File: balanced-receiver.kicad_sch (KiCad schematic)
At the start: 51 parts, among them J1 NC3FAH2, J2 Barrel_Jack_Switch, J3 Screw_Terminal_01x02, J4 Screw_Terminal_01x02, J5 Screw_Terminal_01x02, J6 Screw_Terminal_01x02, J7 Screw_Terminal_01x02, J8 Conn_01x02_Pin, Q1 Q_PMOS_GDS, U1 THAT1240, U2 TPS62932, U3 LM2776

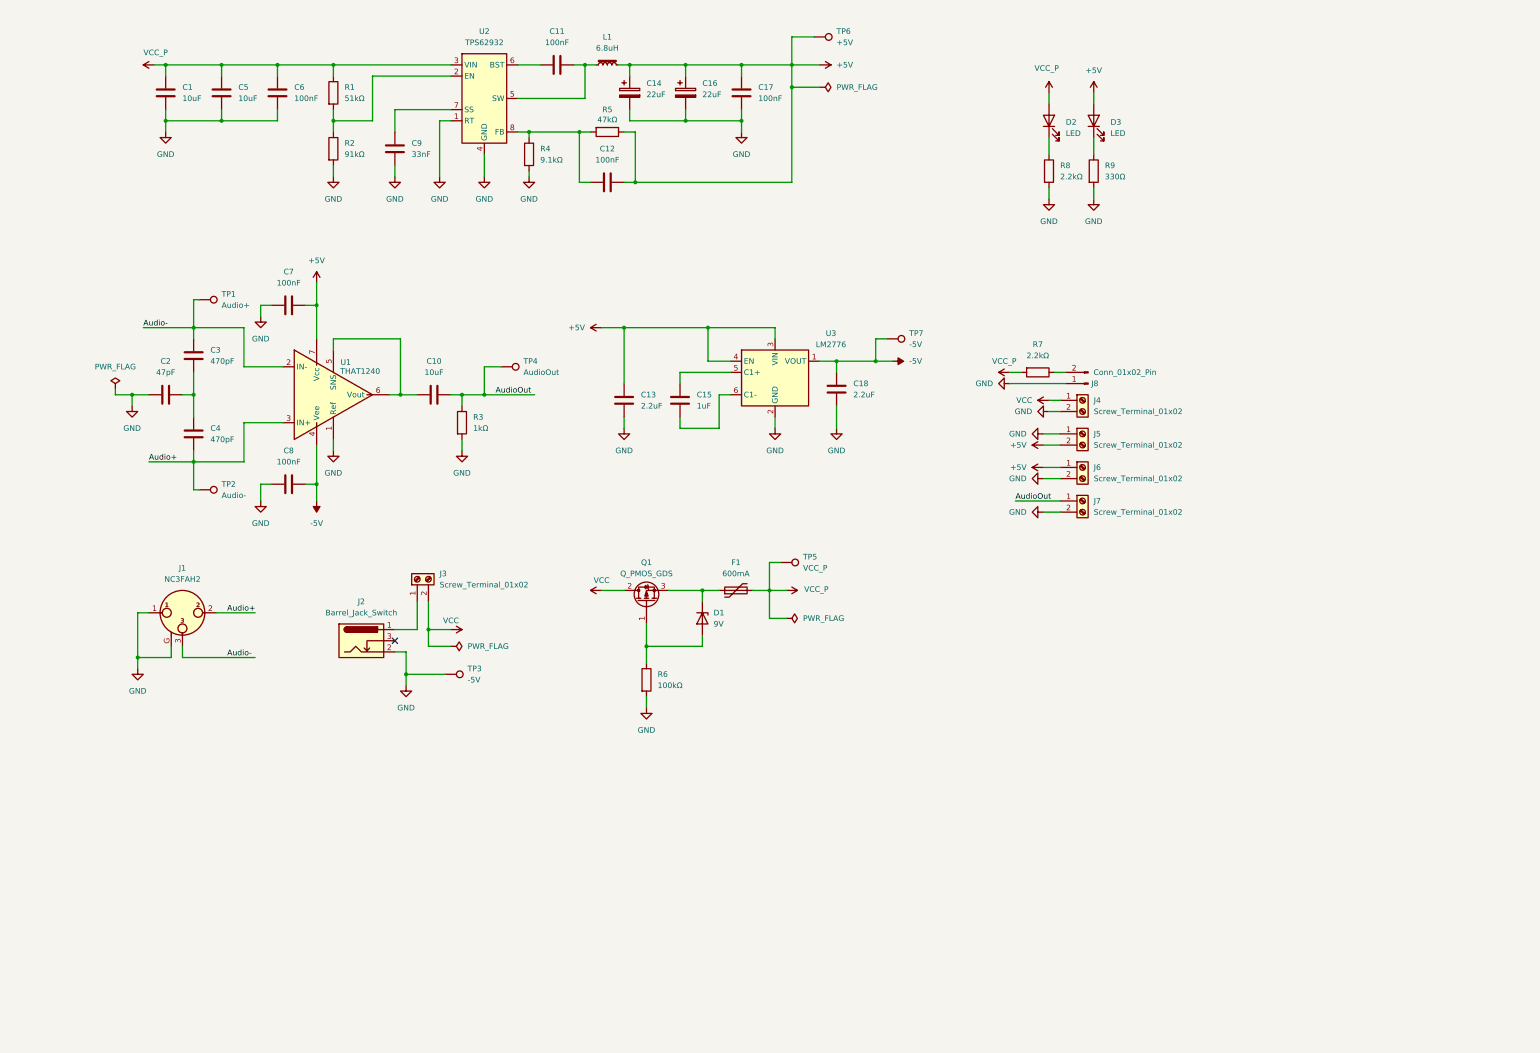
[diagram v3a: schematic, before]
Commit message: Added analog schemas
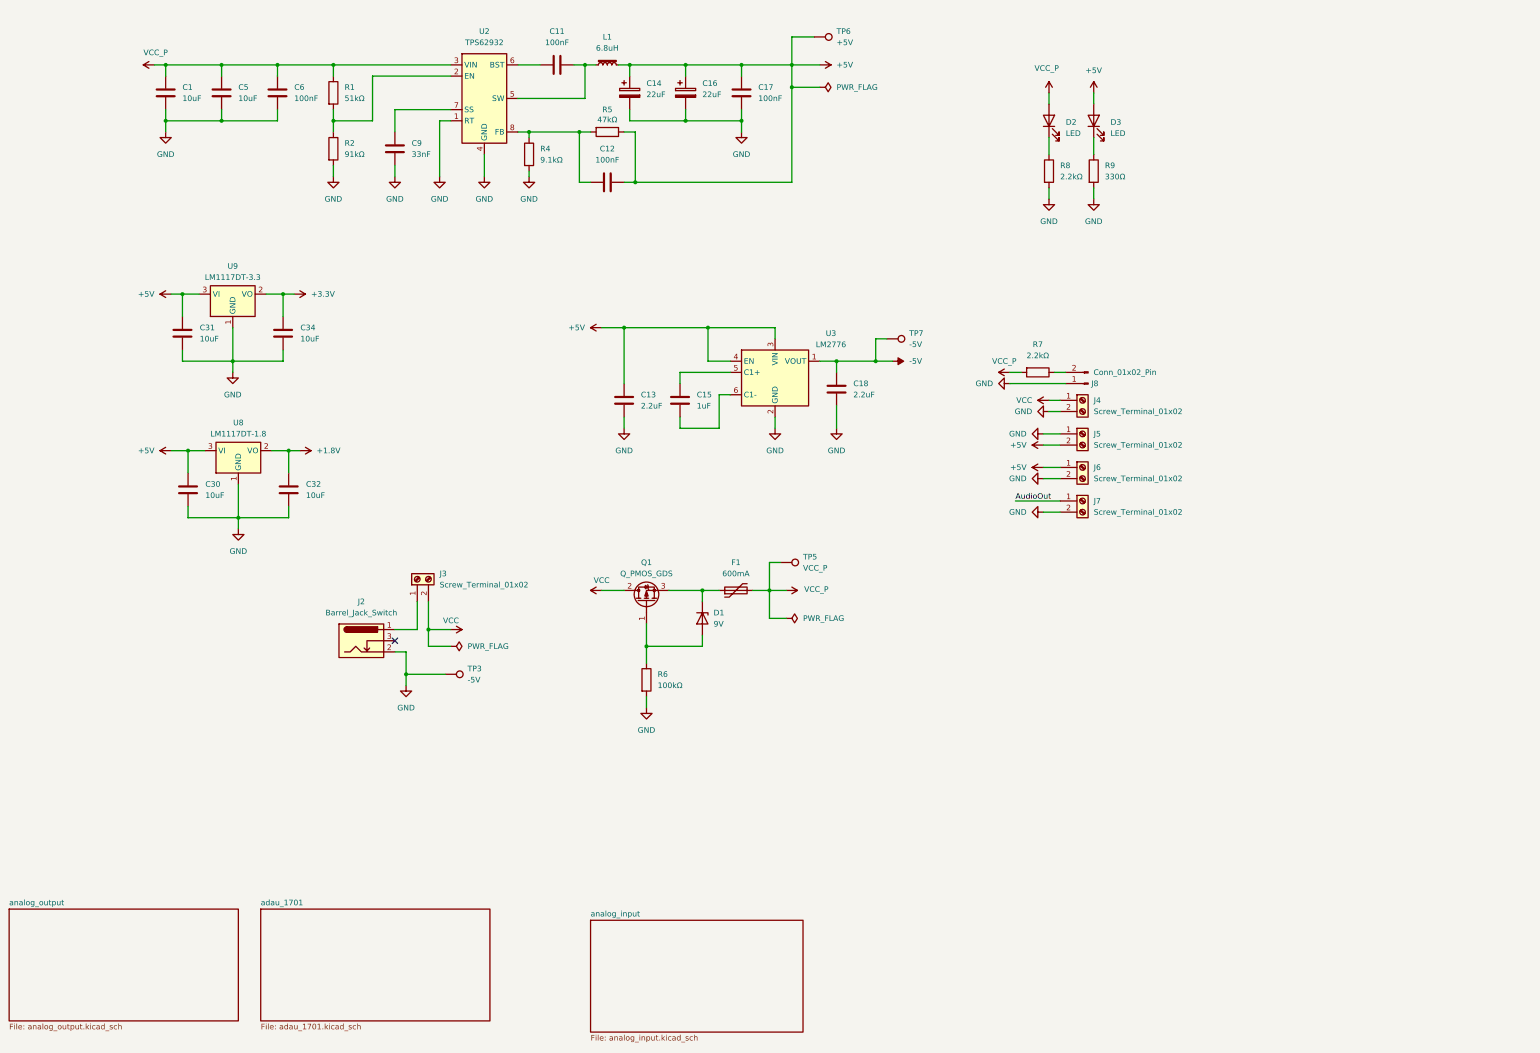
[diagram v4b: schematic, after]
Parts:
- removed C10: 10uF, Capacitor_SMD:C_0805_2012Metric_Pad1.18x1.45mm_HandSolder, symbol Device:C
- removed C2: 47pF, Capacitor_SMD:C_0805_2012Metric_Pad1.18x1.45mm_HandSolder, symbol Device:C
- removed C3, C4: 470pF, Capacitor_SMD:C_0805_2012Metric_Pad1.18x1.45mm_HandSolder, symbol Device:C
- removed C7, C8: 100nF, Capacitor_SMD:C_0805_2012Metric_Pad1.18x1.45mm_HandSolder, symbol Device:C
- removed J1: NC3FAH2, balanced-receiver:Jack_XLR_Neutrik_NC3FAH2_Horizontal, symbol Connector_Audio:NC3FAH2
- removed R3: 1kΩ, Resistor_SMD:R_0805_2012Metric_Pad1.20x1.40mm_HandSolder, symbol Device:R
- removed TP1: Audio+, TestPoint:TestPoint_Pad_D1.0mm, symbol Connector:TestPoint
- removed TP2: Audio-, TestPoint:TestPoint_Pad_D1.0mm, symbol Connector:TestPoint
- removed TP4: AudioOut, TestPoint:TestPoint_Pad_D1.0mm, symbol Connector:TestPoint
- removed U1: THAT1240, Package_SO:SOIC-8_3.9x4.9mm_P1.27mm, symbol balanced-receiver:THAT1240
- added C30, C31, C32, C34: 10uF, Capacitor_SMD:C_0805_2012Metric_Pad1.18x1.45mm_HandSolder, symbol Device:C
- added U8: LM1117DT-1.8, Package_TO_SOT_SMD:TO-252-3_TabPin2, symbol Regulator_Linear:LM1117DT-1.8
- added U9: LM1117DT-3.3, Package_TO_SOT_SMD:TO-252-3_TabPin2, symbol Regulator_Linear:LM1117DT-3.3
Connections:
- net +5V: now also C30.2, C31.2, U8.3 (VI), U9.3 (VI)
- net GND: now also C30.1, C31.1, C32.1, C34.1, U8.1 (GND), U9.1 (GND)
- new net +1.8V: C32.2, U8.2 (VO)
- new net +3.3V: C34.2, U9.2 (VO)
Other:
- added sheet adau_1701 (adau_1701.kicad_sch)
- added sheet analog_input (analog_input.kicad_sch)
- added sheet analog_output (analog_output.kicad_sch)

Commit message: WIP: Converting to schematic
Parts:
- removed D3: LED, LED_SMD:LED_0805_2012Metric_Pad1.15x1.40mm_HandSolder, symbol Device:LED
- removed J4, J6, J7: Screw_Terminal_01x02, TerminalBlock_Phoenix:TerminalBlock_Phoenix_MPT-0,5-2-2.54_1x02_P2.54mm_Horizontal, symbol Connector:Screw_Terminal_01x02
- removed J8: Conn_01x02_Pin, Connector_PinHeader_2.54mm:PinHeader_1x02_P2.54mm_Vertical, symbol Connector:Conn_01x02_Pin
- removed R7: 2.2kΩ, Resistor_SMD:R_0805_2012Metric_Pad1.20x1.40mm_HandSolder, symbol Device:R
- removed R9: 330Ω, Resistor_SMD:R_0805_2012Metric_Pad1.20x1.40mm_HandSolder, symbol Device:R
- removed TP3, TP7: -5V, TestPoint:TestPoint_Pad_D1.0mm, symbol Connector:TestPoint
- removed TP6: +5V, TestPoint:TestPoint_Pad_D1.0mm, symbol Connector:TestPoint
- added C58, C59: 10uF, Capacitor_SMD:C_0805_2012Metric_Pad1.18x1.45mm_HandSolder, symbol Device:C
- added J4: Screw_Terminal_01x03, balanced-receiver:TerminalBlock_1x03_P7.50mm_Horizontal, symbol Connector:Screw_Terminal_01x03
- added L2, L3: 1uH, Inductor_SMD:L_0805_2012Metric_Pad1.05x1.20mm_HandSolder, symbol Device:L
- J2: renamed from J3; footprint TerminalBlock_Phoenix:TerminalBlock_Phoenix_MPT-0,5-2-2.54_1x02_P2.54mm_Horizontal -> balanced-receiver:TerminalBlock_Phoenix_MPT-0,5-2-2.54_1x02_P2.54mm_Horizontal
- L1: footprint balanced-receiver:L_7.3x7.3_H4.5 -> Inductor_SMD:L_APV_APH0530
- U1: renamed from U9; footprint Package_TO_SOT_SMD:TO-252-3_TabPin2 -> Package_TO_SOT_SMD:SOT-223-3_TabPin2
- U2: renamed from U8; footprint Package_TO_SOT_SMD:TO-252-3_TabPin2 -> Package_TO_SOT_SMD:SOT-223-3_TabPin2
- U4: renamed from U3; footprint Package_TO_SOT_SMD:SOT-23-6 -> Package_TO_SOT_SMD:SOT-23-6_Handsoldering
- renumbered C11 to C10, C15 to C11, C14 to C13, C16 to C14, C17 to C15, C18 to C16, C31 to C2, C30 to C3, C5 to C4, C6 to C5, C34 to C6, C32 to C7, C9 to C8, C13 to C9, J2 to J1, J5 to J3, R4 to R3, R6 to R4, R8 to R7, TP5 to TP2, U2 to U3
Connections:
- net +5V: now also L2.1
- net -5V: now also C59.1, L3.2; no longer C16.1, U4.1 (VOUT)
- net GND: now also C58.2, C59.2, J4.1 (Pin_1)
- net VCC_P: now also J4.3 (Pin_3)
- net VCC_UN: now reaches J1.1, J2.1 (Pin_1)
- net VCC_UN: now also J4.2 (Pin_2)
- new net: C16.1, L3.1, U4.1 (VOUT)
- new net +5V_ANALOG: C58.1, L2.2
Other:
- moved on the sheet: C11, C16, C2, C3, C6, C7, C9, D1, F1, J1, J2, J3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

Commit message: WIP
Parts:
- removed C10, C15: 100nF, Capacitor_SMD:C_0805_2012Metric_Pad1.18x1.45mm_HandSolder, symbol Device:C
- removed C16, C9: 2.2uF, Capacitor_SMD:C_0805_2012Metric_Pad1.18x1.45mm_HandSolder, symbol Device:C
- removed C58, C59, C7: 10uF, Capacitor_SMD:C_0805_2012Metric_Pad1.18x1.45mm_HandSolder, symbol Device:C
- removed C8: 33nF, Capacitor_SMD:C_0805_2012Metric_Pad1.18x1.45mm_HandSolder, symbol Device:C
- removed J1: Barrel_Jack_Switch, balanced-receiver:BarrelJack_GCT_DCJ200-10-A_Horizontal, symbol Connector:Barrel_Jack_Switch
- removed J2: Screw_Terminal_01x02, balanced-receiver:TerminalBlock_Phoenix_MPT-0,5-2-2.54_1x02_P2.54mm_Horizontal, symbol Connector:Screw_Terminal_01x02
- removed J4: Screw_Terminal_01x03, balanced-receiver:TerminalBlock_1x03_P7.50mm_Horizontal, symbol Connector:Screw_Terminal_01x03
- removed L2, L3: 1uH, Inductor_SMD:L_0805_2012Metric_Pad1.05x1.20mm_HandSolder, symbol Device:L
- removed R1: 51kΩ, Resistor_SMD:R_0805_2012Metric_Pad1.20x1.40mm_HandSolder, symbol Device:R
- removed TP2: VCC_P, TestPoint:TestPoint_Pad_D1.0mm, symbol Connector:TestPoint
- removed U2: LM1117DT-1.8, Package_TO_SOT_SMD:SOT-223-3_TabPin2, symbol Regulator_Linear:LM1117DT-1.8
- removed U3: TPS62932, balanced-receiver:SOT-583-8, symbol Regulator_Switching:TPS62932
- removed U4: LM2776, Package_TO_SOT_SMD:SOT-23-6_Handsoldering, symbol Regulator_SwitchedCapacitor:LM2776
- added C2: 10uF, Capacitor_SMD:C_0805_2012Metric_Pad1.18x1.45mm_HandSolder, symbol Device:C
- added C6: 10nF, Capacitor_SMD:C_0805_2012Metric_Pad1.18x1.45mm_HandSolder, symbol Device:C
- added C7, C8: 220uF, Capacitor_SMD:CP_Elec_6.3x7.7, symbol Device:C_Polarized
- added D2, D3: B340A, Diode_SMD:D_SMA_Handsoldering, symbol Device:D
- added H1, H2, H3, H4: MountingHole_Pad_MP, MountingHole_2.2mm_M2_DIN965_Pad_TopBottom, symbol Mechanical:MountingHole_Pad_MP
- added J1: Power, Connector_JST:JST_XH_B2B-XH-A_1x02_P2.50mm_Vertical, symbol Connector:Conn_01x02_Pin
- added L2: 22uH, Inductor_SMD:L_APV_ANR6028, symbol Device:L_Iron_Small
- added L3, L4: 1uH, Inductor_SMD:L_APV_APH0420, symbol Device:L_Iron_Small
- added R4: 10kΩ, Resistor_SMD:R_0805_2012Metric_Pad1.20x1.40mm_HandSolder, symbol Device:R
- added U1, U2: TPS5430DDA, Package_SO:TI_SO-PowerPAD-8, symbol Regulator_Switching:TPS5430DDA
- C11: value 1uF -> 22pF
- C12: value 100nF -> 22pF
- C5: value 100nF -> 10nF
- L1: value 6.8uH -> 22uH; footprint Inductor_SMD:L_APV_APH0530 -> Inductor_SMD:L_APV_ANR6028
- R2: value 91kΩ -> 10kΩ
- R3: value 9.1kΩ -> 3.3k
- R5: value 47kΩ -> 3.3kΩ
- renumbered C2 to C15, C6 to C16, D2 to D4, J3 to J2, R4 to R1, R7 to R6, U1 to U3
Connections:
- net +5V: now also L3.2; no longer C12.2, C14.1, C3.2, L1.2, R5.1
- net -5V: now also C14.2, L4.2
- net GND: now also C12.1, C14.1, C3.2, C2.2, C7.2, C8.1, D2.2 (A), H1.MP, H2.MP, H3.MP, H4.MP, J1.2 (Pin_2), L2.2, R4.2, U1.6 (GND), U1.9 (GNDPAD); no longer C14.2, C3.1, C4.2, C5.2, R2.2
- net VCC: now also C1.1, C3.1, C4.1, D4.2 (A), F1.2, C2.1, U1.7 (VIN), U2.7 (VIN); no longer Q1.2 (D)
- net at R2.1: now also C11.2, R3.1, U1.4 (VSENSE)
- net at L1.1: now also C5.2, D2.1 (K), U1.8 (PH)
- net at C11.1: now also L1.2, R2.2, C7.1, L3.1
- removed net VCC_P: C1.1, C4.1, C5.1, D4.2 (A), F1.2
- new net: C12.2, R4.1, R5.1, U2.4 (VSENSE)
- new net: C4.2, C8.2, D3.2 (A), L4.1, R5.2, U2.6 (GND), U2.9 (GNDPAD)
- new net: J1.1 (Pin_1), Q1.2 (D)
- new net: C6.1, U2.1 (BOOT)
- new net: C6.2, D3.1 (K), L2.1, U2.8 (PH)
- new net: C5.1, U1.1 (BOOT)
- no-connect marks 1 -> 2
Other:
- moved on the sheet: C15, C16, D1, D4, F1, J2, Q1, R1, R6, U3

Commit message: Completed PCB
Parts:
- Q1: footprint Package_TO_SOT_SMD:SOT-23 -> Package_TO_SOT_SMD:SOT-223-3_TabPin2
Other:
- moved on the sheet: C13, C15, C16, U3
